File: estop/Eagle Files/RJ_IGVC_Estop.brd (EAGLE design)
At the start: 57 x 46 mm, 29 parts, among them T1 TRANSISTOR, T2 LD1086D2M33TR, U4 ATMEGA328P-AUR, X1 2X3SHROUDED, X2 1751248, X3 1751248, X4 1751248, X5 1751248

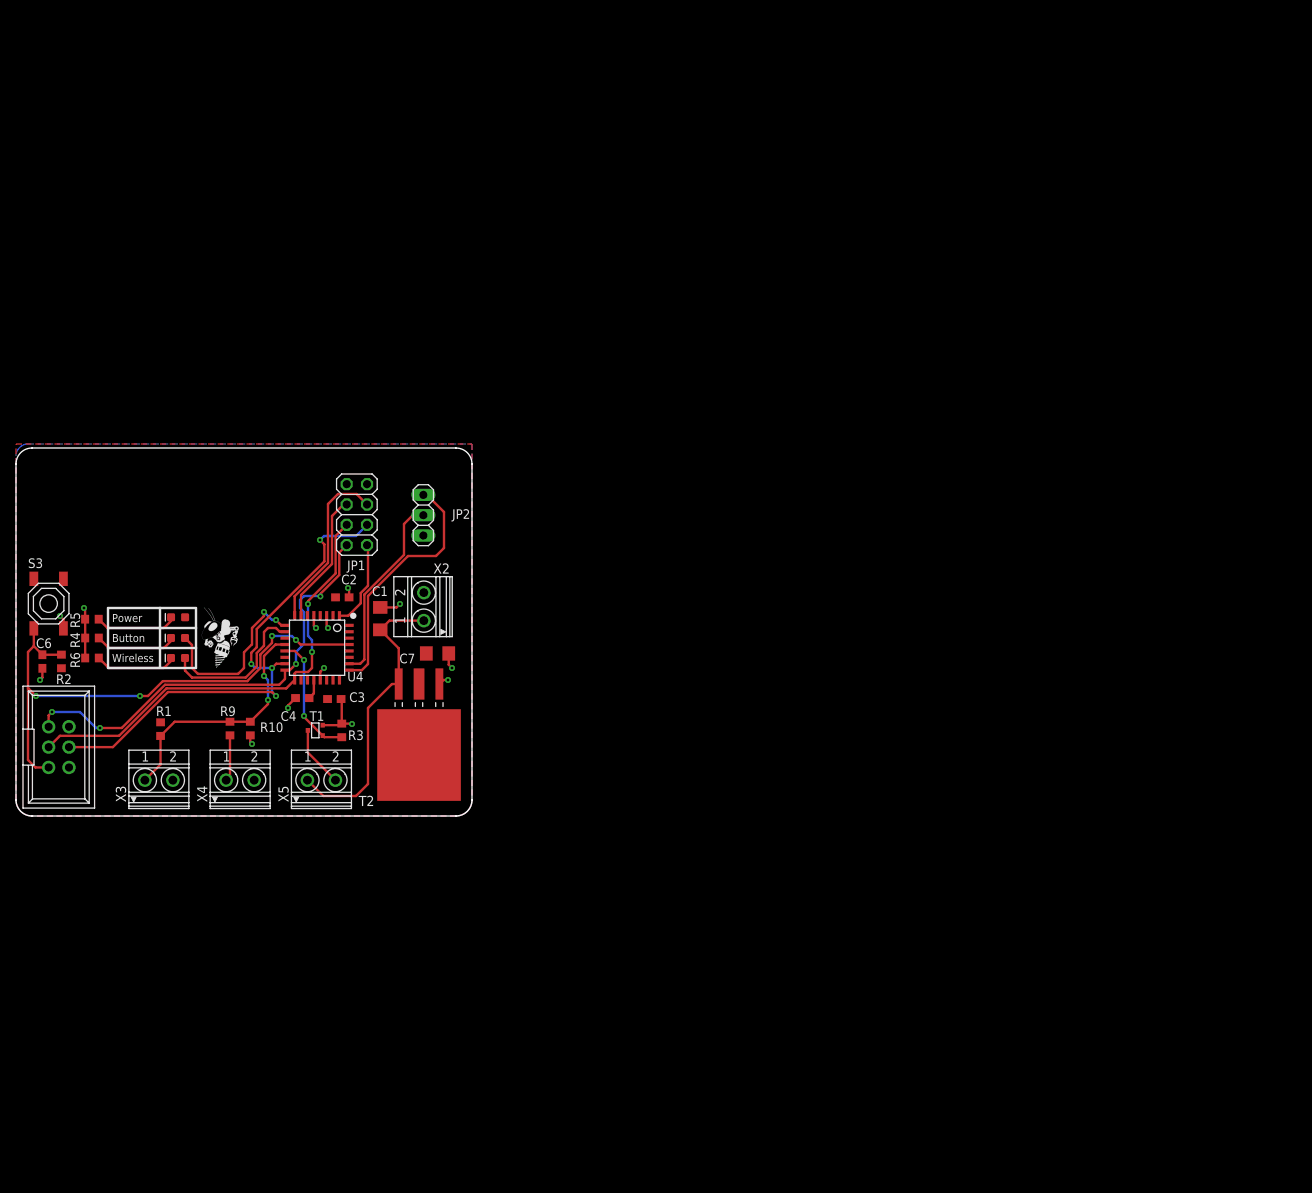
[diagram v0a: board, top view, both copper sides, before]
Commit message: New relay estop
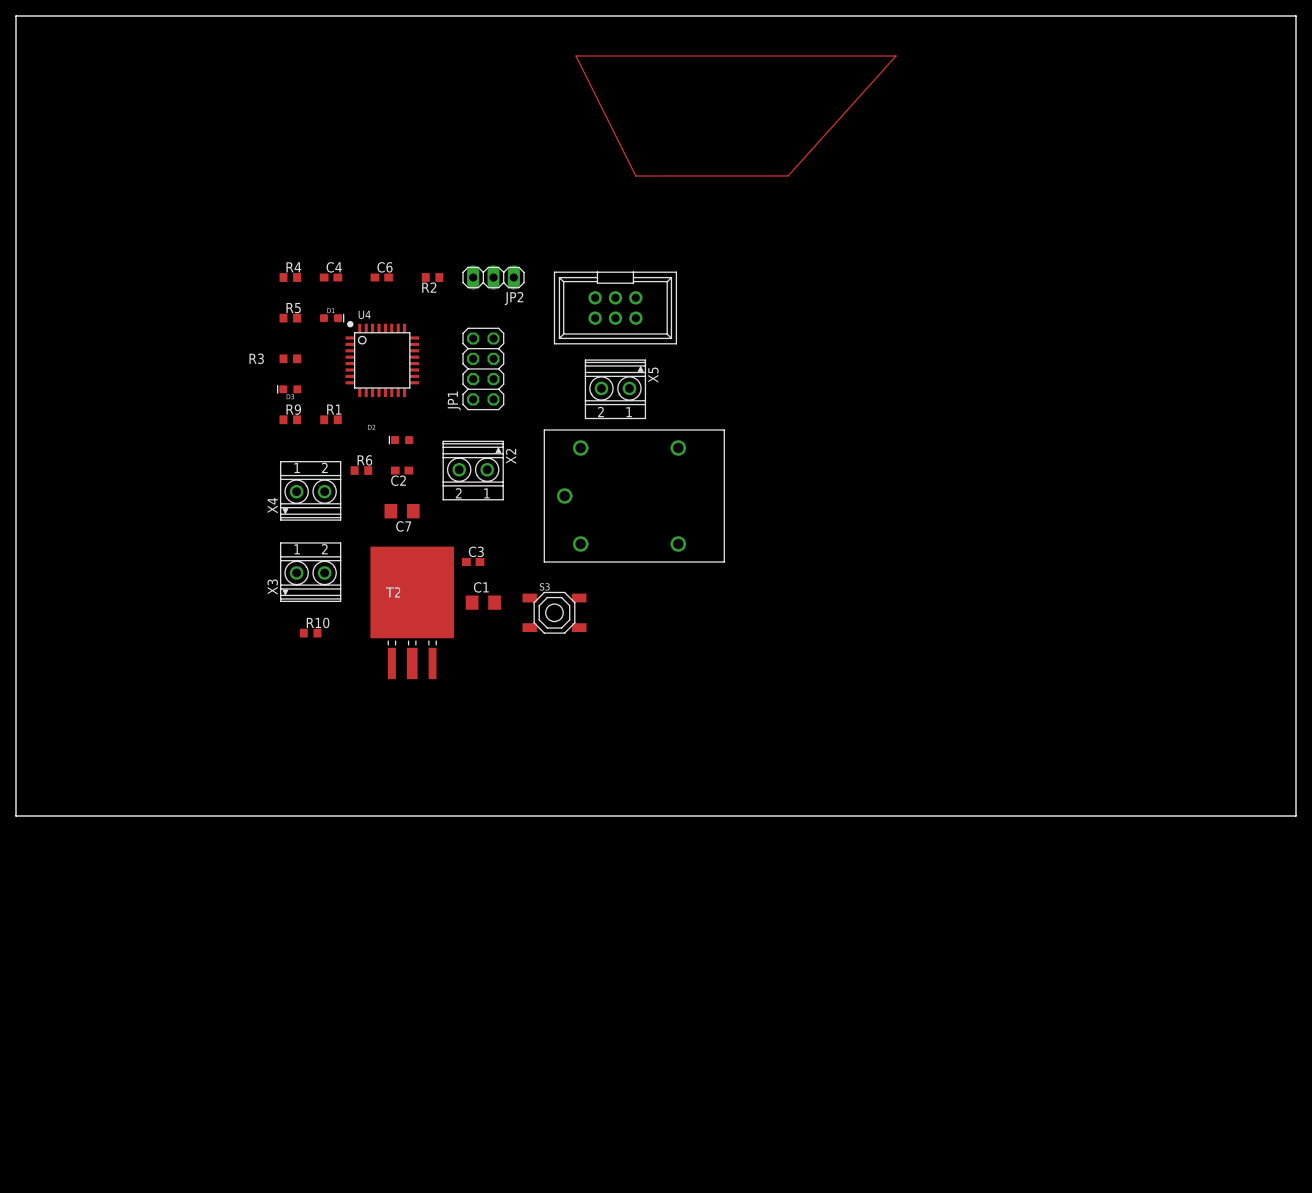
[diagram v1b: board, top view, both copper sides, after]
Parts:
- removed T1: TRANSISTOR, transistor:SC70
- removed U$2: (no value), RoboJackets-Aesthetics:ROBOBUZZ_0.4X
- added U$1: G5LE-14, IGVC-Misc:G5LE-14
- moved X1 88.6 mm to (74.9, 63.5), turned to 0 degrees
- moved R2 66.7 mm to (52.1, 67.3), turned to 180 degrees
- moved C6 64.1 mm to (45.7, 67.3), turned to 0 degrees
- moved S3 63.2 mm to (67.3, 25.4), turned to 0 degrees
- moved X5 61.1 mm to (74.9, 53.3), turned to 180 degrees
- moved C4 52.7 mm to (39.4, 67.3), turned to 0 degrees
- moved R4 51.4 mm to (34.3, 67.3)
- moved R3 46.9 mm to (34.3, 57.1), turned to 180 degrees
- moved R5 45.1 mm to (34.3, 62.2)
- moved D1 44.3 mm to (39.4, 62.2), turned to 0 degrees
- moved R1 44.1 mm to (39.4, 49.5), turned to 0 degrees
- moved R6 41.0 mm to (43.2, 43.2)
- moved R9 39.3 mm to (34.3, 49.5), turned to 0 degrees
- moved X4 37.1 mm to (36.8, 40.6)
- moved U4 36.9 mm to (45.7, 57.1), turned to 0 degrees
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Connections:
- new net N$5: U$1.P$4, X5.2
- net GND: now also U$1.P$5; no longer T1.2
- net N$1: now also U$1.P$1, U$1.P$3, X5.1; no longer T1.3, X5.2
- net OUT: now also U$1.P$2; no longer T1.1
- net V_IN: no longer X5.1
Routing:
- net N$10: track 0.00 -> 96.0 mm
- net !RESET: track 69.2 -> 0.00 mm, vias 4 -> 0
- net MOSI: track 63.5 -> 0.00 mm, vias 4 -> 0
- net SCK: track 57.6 -> 0.00 mm, vias 2 -> 0
- net MISO: track 56.5 -> 0.00 mm, vias 4 -> 0
- net V_IN: track 37.2 -> 0.00 mm
- net GND: track 31.4 -> 0.00 mm, vias 13 -> 0
- net N$7: track 31.1 -> 0.00 mm
- net IN: track 30.9 -> 0.00 mm, vias 2 -> 0
- net N$8: track 24.0 -> 0.00 mm
- net BUTTON_LED: track 22.6 -> 0.00 mm, vias 2 -> 0
- net CSN: track 21.6 -> 0.00 mm
- net WIRELESS_LED: track 19.2 -> 0.00 mm
- net CE: track 16.5 -> 0.00 mm
- net OUT: track 15.7 -> 0.00 mm, vias 2 -> 0
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- removed copper zone on layer 1, net +3.3V
- removed copper zone on layer 16, net GND
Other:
- board size 57 x 46 mm -> 160 x 100 mm
- board text removed: "Button"
- board text removed: "E-Stop Board v1.0"
- board text removed: "Power"
- board text removed: "Wireless"

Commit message: Estop routingstarted
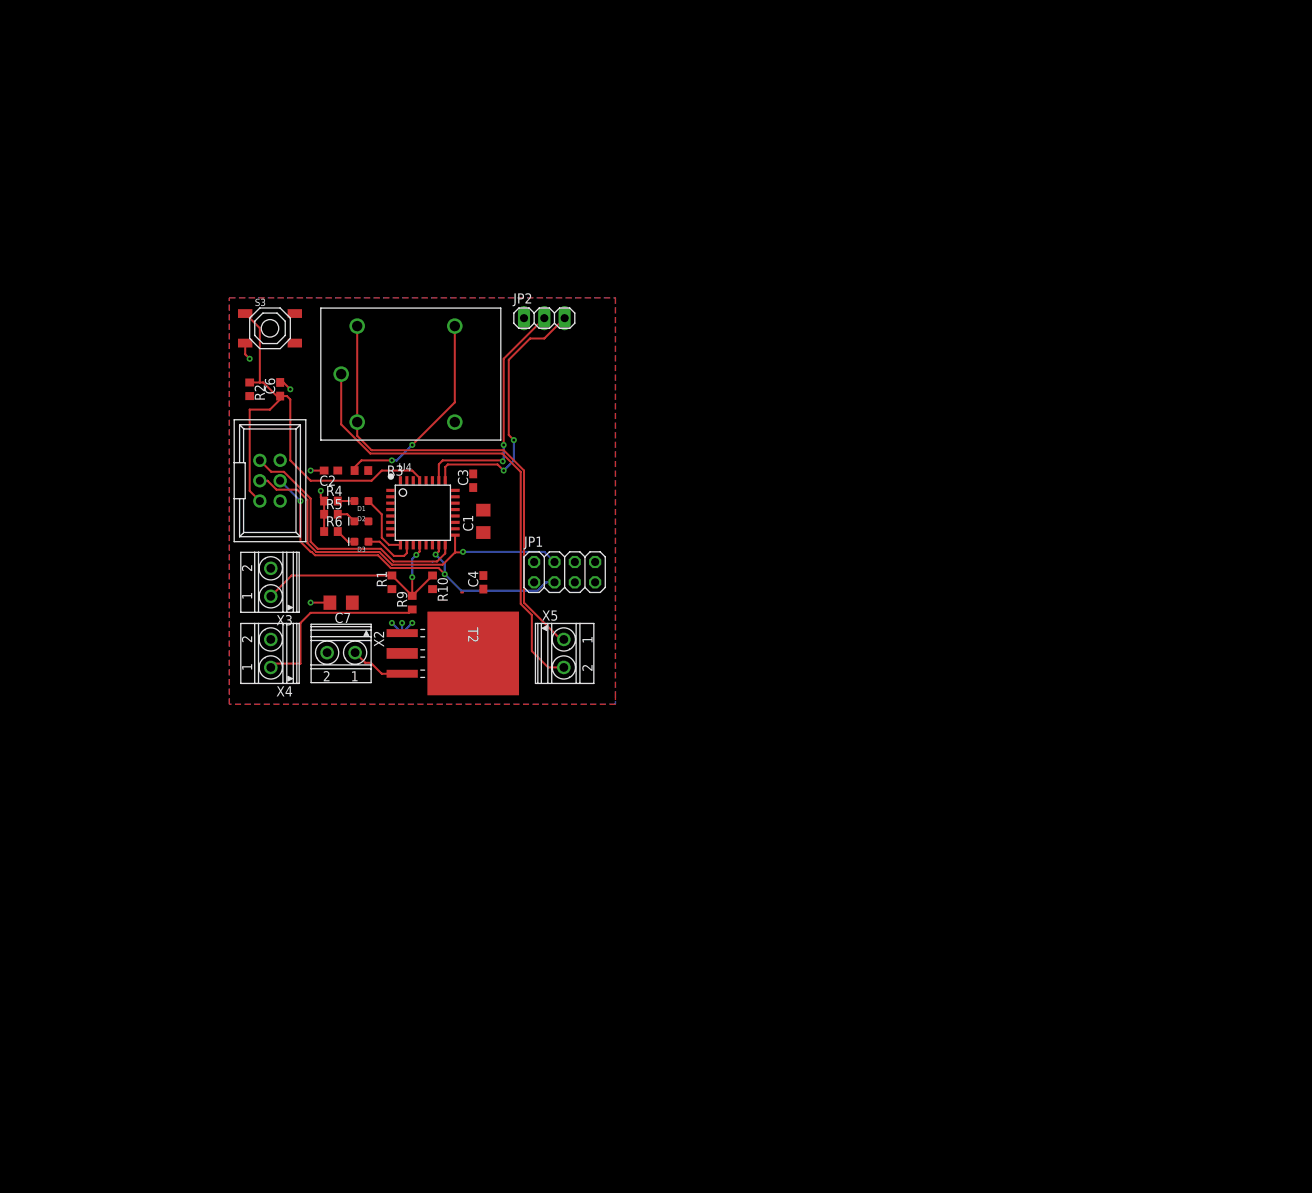
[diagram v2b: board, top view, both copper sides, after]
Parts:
- moved S3 50.3 mm to (31.8, 61.0)
- moved X1 48.3 mm to (31.8, 41.9), turned to 90 degrees
- moved C4 42.6 mm to (58.4, 29.2), turned to 90 degrees
- moved X5 33.6 mm to (68.6, 20.3), turned to 270 degrees
- moved U$1 31.8 mm to (38.1, 47.0)
- moved R4 28.4 mm to (39.4, 39.4)
- moved X2 28.2 mm to (40.6, 20.3)
- moved R9 27.5 mm to (49.5, 26.7), turned to 90 degrees
- moved JP1 27.4 mm to (68.6, 30.5), turned to 0 degrees
- moved R2 26.8 mm to (29.2, 53.3), turned to 270 degrees
- moved R5 25.0 mm to (39.4, 37.7)
- moved D1 23.2 mm to (43.2, 39.4), turned to 180 degrees
- moved R1 21.7 mm to (47.0, 29.2), turned to 90 degrees
- moved D3 21.0 mm to (43.2, 34.3)
- moved X4 20.9 mm to (31.8, 20.3), turned to 90 degrees
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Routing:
- net N$10: track 96.0 -> 0.00 mm
- net N$1: track 0.00 -> 59.8 mm
- net N$5: track 0.00 -> 59.0 mm
- net !RESET: track 0.00 -> 57.9 mm
- net SCK: track 0.00 -> 48.2 mm, vias 0 -> 1
- net MOSI: track 0.00 -> 47.7 mm, vias 0 -> 3
- net N$7: track 0.00 -> 33.2 mm, vias 0 -> 2
- net MISO: track 0.00 -> 33.1 mm
- net N$8: track 0.00 -> 30.3 mm, vias 0 -> 2
- net IN: track 0.00 -> 30.2 mm, vias 0 -> 2
- net OUT: track 0.00 -> 25.8 mm, vias 0 -> 2
- net N$6: track 0.00 -> 23.7 mm
- net GND: track 0.00 -> 18.0 mm, vias 0 -> 8
- net BUTTON_LED: track 0.00 -> 7.97 mm
- net V_IN: track 0.00 -> 6.98 mm
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- added copper zone on layer 1, net +3.3V
- added copper zone on layer 16, net GND
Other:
- board outline removed

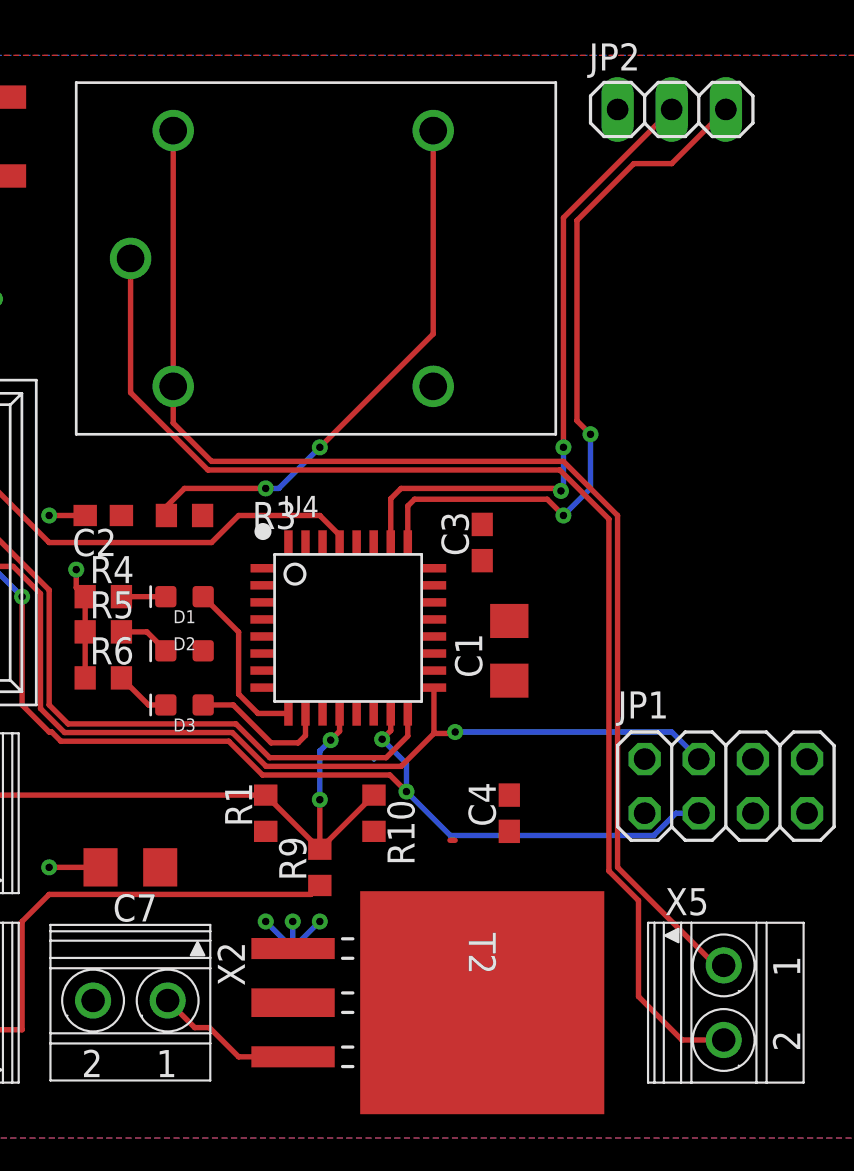
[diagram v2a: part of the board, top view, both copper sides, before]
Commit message: fixed relay connections
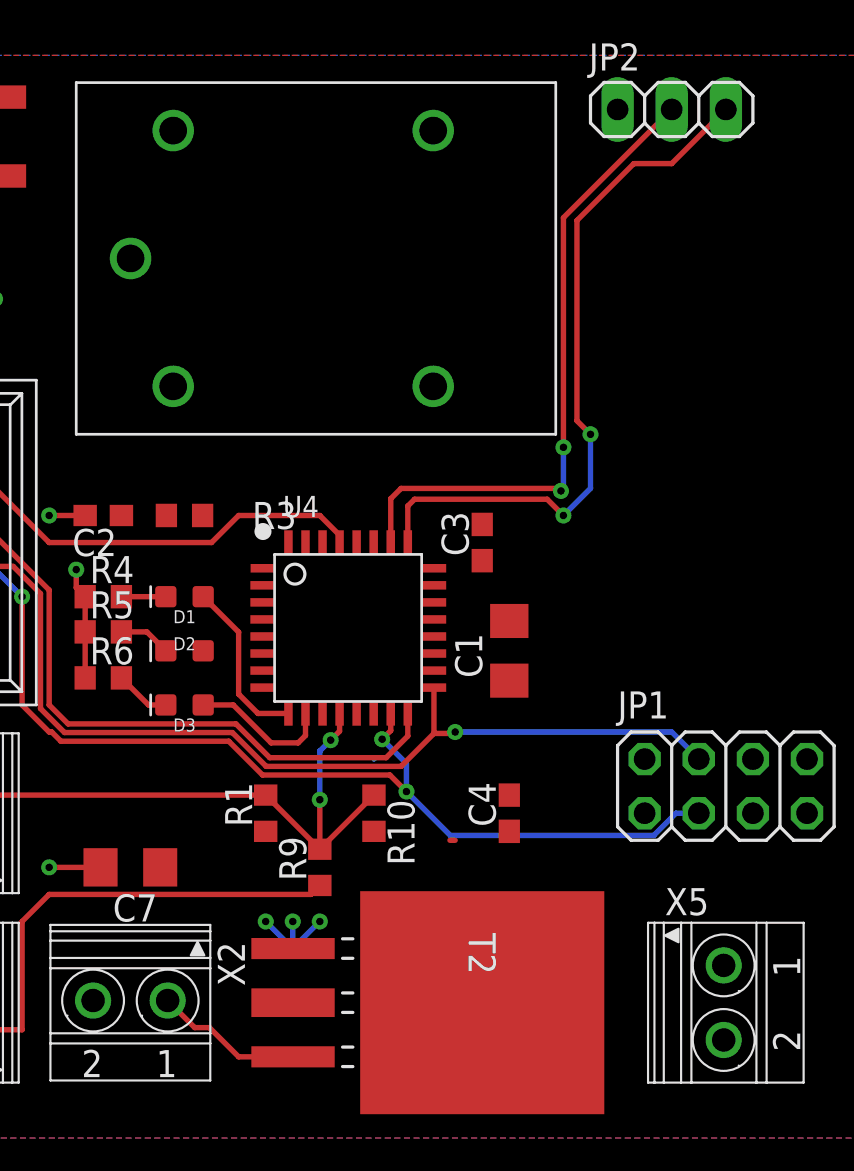
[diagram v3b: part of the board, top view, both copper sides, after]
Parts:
- JP1: value (none) -> NRF24L01+PA+LNA
- JP2: value (none) -> Serial
- X1: value 2X3SHROUDED -> ICSP Connector
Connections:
- net +3.3V renamed +3V3
- removed net N$1: U$1.P$1, U$1.P$3, X5.1
- new net N$10: U$1.P$2, U$1.P$4, X5.1
- net GND: now also R3.1, U$1.P$1; no longer R3.2, U$1.P$5
- net N$5: now also U$1.P$5; no longer U$1.P$4
- net OUT: now also R3.2, U$1.P$3; no longer R3.1, U$1.P$2
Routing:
- net N$1: track 59.8 -> 0.00 mm
- net N$5: track 59.0 -> 0.00 mm
- net OUT: track 25.8 -> 0.00 mm, vias 2 -> 0

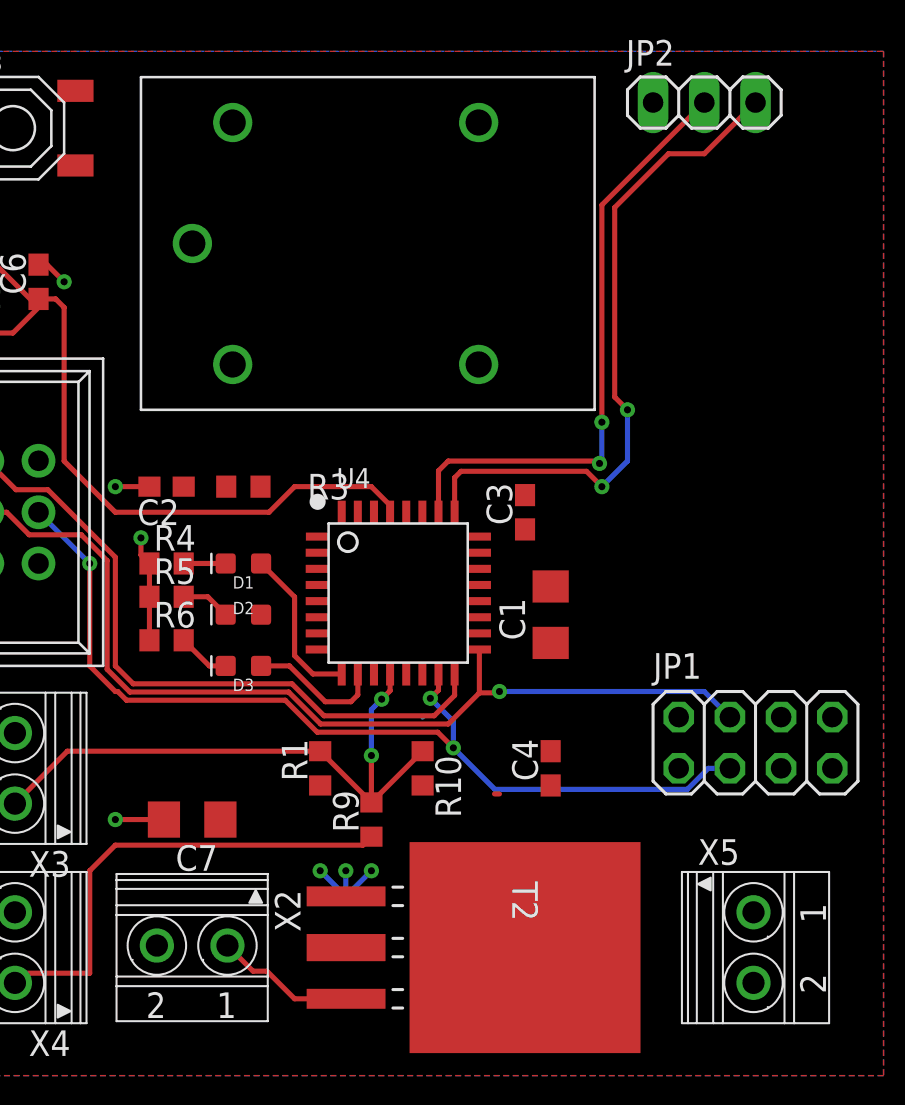
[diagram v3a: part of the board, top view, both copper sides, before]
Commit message: estop board - not completely finished...
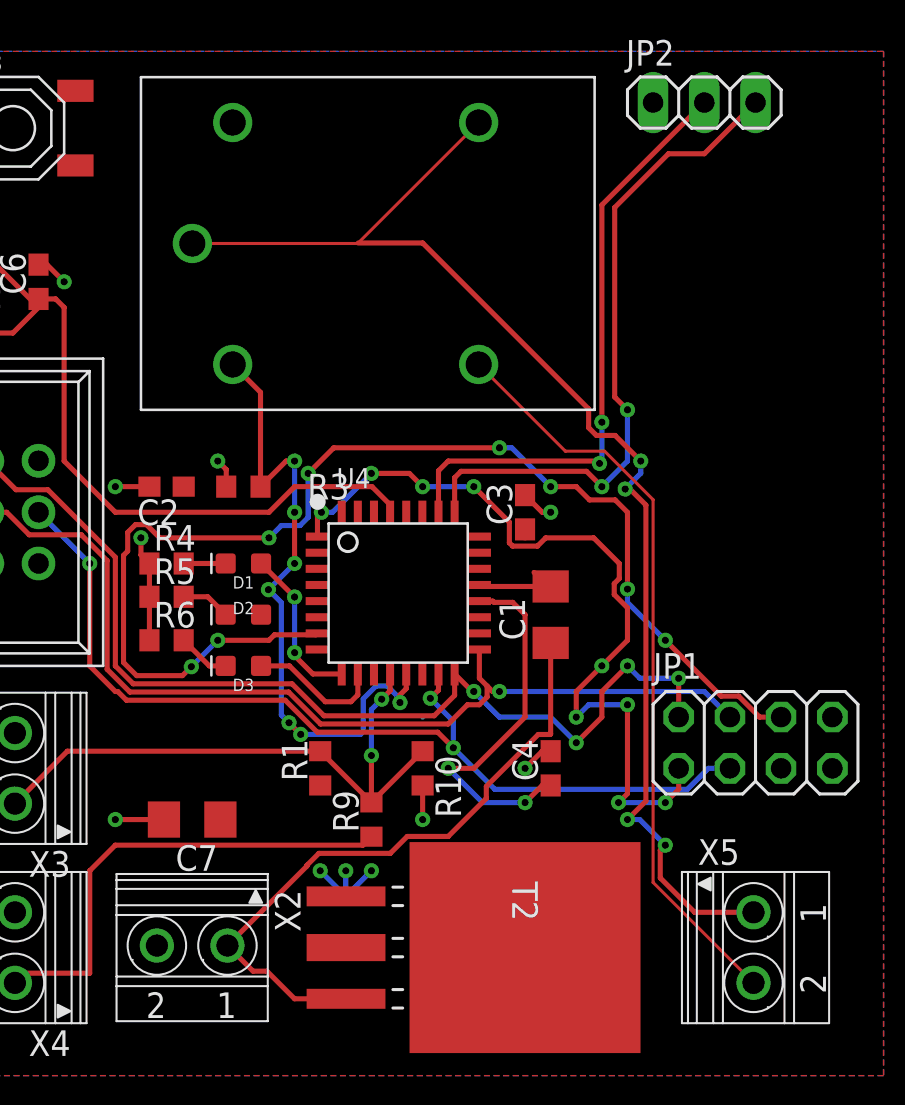
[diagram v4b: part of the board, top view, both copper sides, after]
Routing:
- net N$10: track 0.00 -> 64.3 mm, vias 0 -> 4
- net CE: track 0.00 -> 61.4 mm, vias 0 -> 8
- net IRQ: track 0.00 -> 40.8 mm, vias 0 -> 9
- net N$5: track 0.00 -> 37.5 mm
- net OUT: track 0.00 -> 32.5 mm, vias 0 -> 7
- net V_IN: track 6.98 -> 32.2 mm
- net N$9: track 0.00 -> 18.6 mm, vias 0 -> 2
- net MISO: track 33.1 -> 50.1 mm, vias 0 -> 4
- net GND: track 18.0 -> 29.3 mm, vias 8 -> 12
- net BUTTON_LED: vias 0 -> 2
